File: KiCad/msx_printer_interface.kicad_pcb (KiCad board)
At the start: 2 copper layers, 65.7 x 54 mm, 12 parts, among them J1 MSX Cartridge Connector, J2 Conn_02x07_Top_Bottom, U1 ATF22V10C-15PU, U2 74HC273

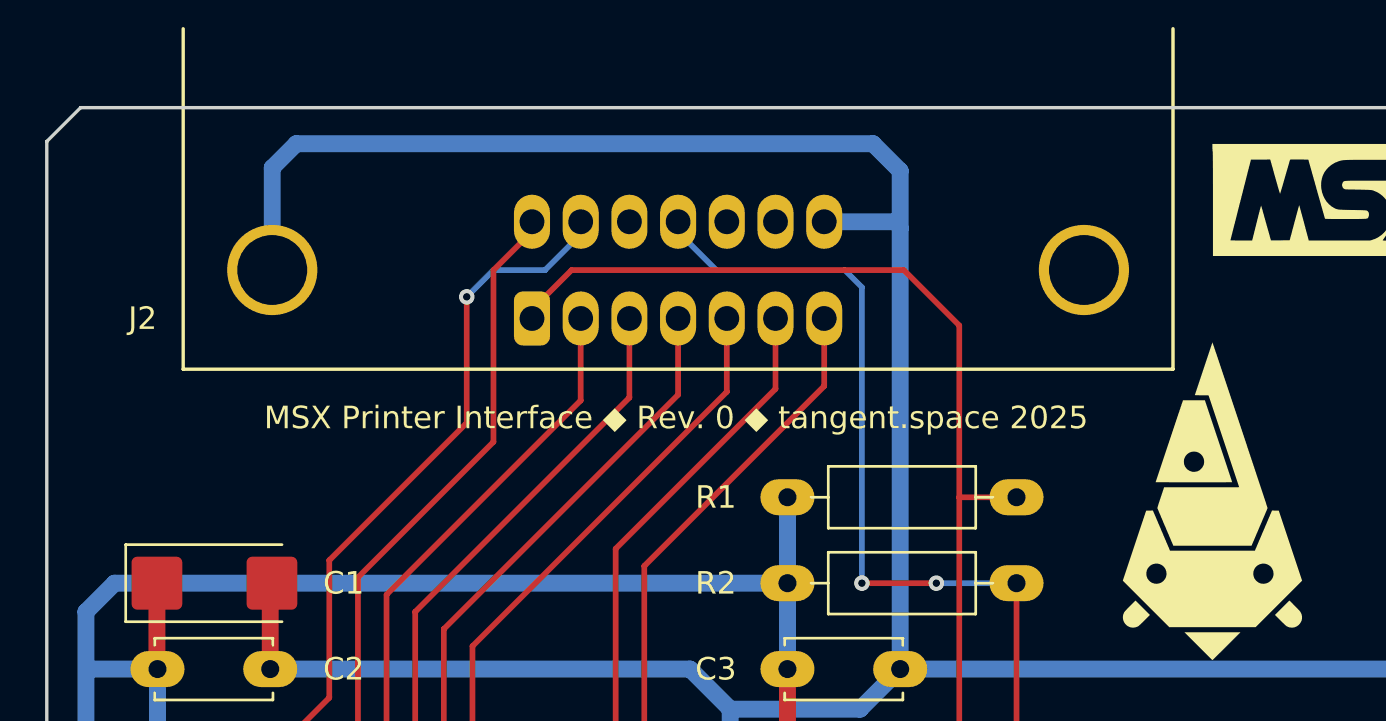
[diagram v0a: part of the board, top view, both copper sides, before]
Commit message: Adjust J2 ground
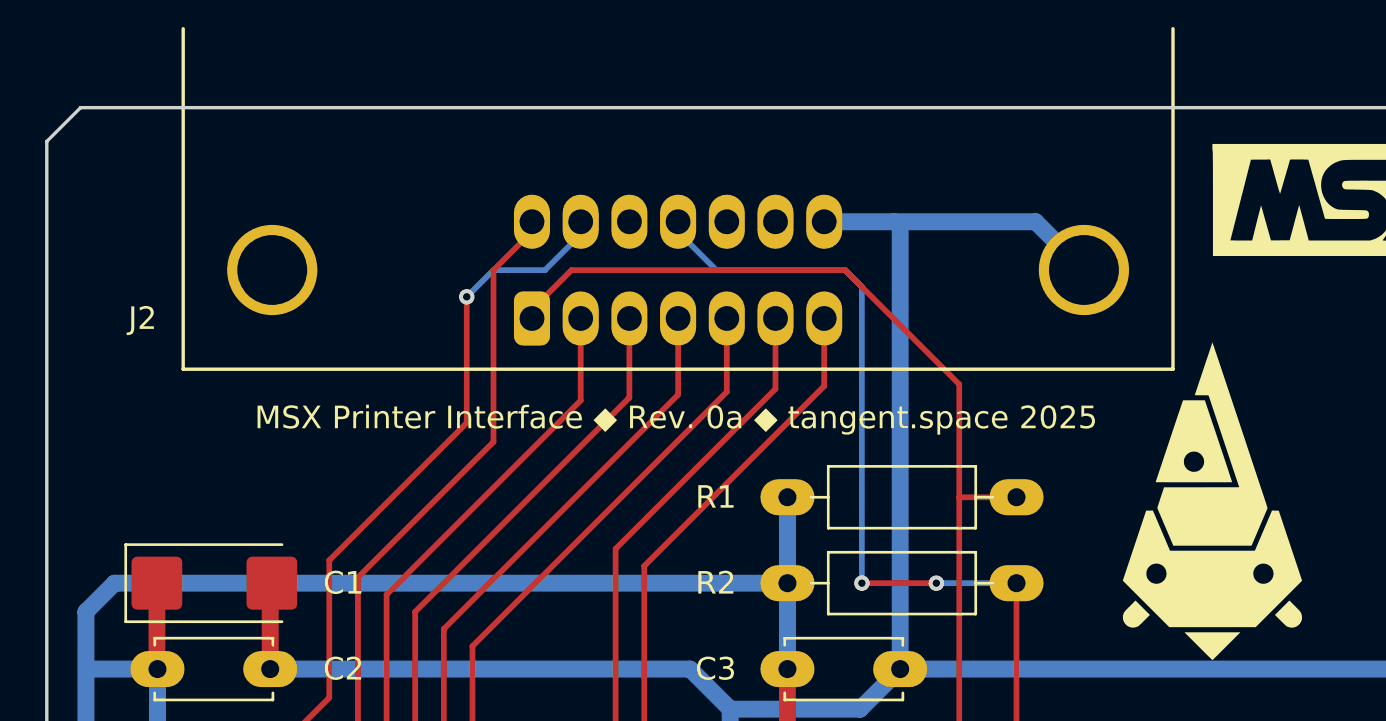
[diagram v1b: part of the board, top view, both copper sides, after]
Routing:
- net GND: track 180.1 -> 153.6 mm
- net #STROBE: track 42.3 -> 40.8 mm
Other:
- board text added: "MSX Printer Interface ◆ Rev. 0a ◆ tangent.space 2025"
- board text removed: "MSX Printer Interface ◆ Rev. 0 ◆ tangent.space 2025"
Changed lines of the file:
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@@
 			(layers "*.Cu" "*.Mask")
 			(remove_unused_layers no)
-			(net 2 "GND")
 		)
 		(pad "" thru_hole circle
@@
 			(layers "*.Cu" "*.Mask")
 			(remove_unused_layers no)
+			(net 2 "GND")
 		)
 		(pad "1" thru_hole roundrect
@@
 		(layer "Edge.Cuts")
 	)
-	(gr_text "MSX Printer Interface ◆ Rev. 0 ◆ tangent.space 2025"
+	(gr_text "MSX Printer Interface ◆ Rev. 0a ◆ tangent.space 2025"
 		(at 54.4125 17.255 0)
 		(layer "F.SilkS")
@@
 	)
 	(segment
-		(start 37.565 5.1)
-		(end 63.148 5.1)
-		(width 0.75)
-		(layer "B.Cu")
-		(net 2)
-	)
-	(segment
 		(start 37.795 44.875)
 		(end 39.03 43.64)
@@
 	)
 	(segment
-		(start 36.5 10.7)
-		(end 36.5 6.165)
+		(start 39.03 43.64)
+		(end 54.25 43.64)
 		(width 0.75)
 		(layer "B.Cu")
@@
 	)
 	(segment
-		(start 39.03 43.64)
-		(end 54.25 43.64)
+		(start 56.81 42.37)
+		(end 56.81 39.83)
 		(width 0.75)
 		(layer "B.Cu")
@@
 	)
 	(segment
-		(start 56.81 42.37)
-		(end 56.81 39.83)
+		(start 64.068 8.56)
+		(end 70.36 8.56)
 		(width 0.75)
 		(layer "B.Cu")
@@
 	)
 	(segment
+		(start 70.36 8.56)
+		(end 72.5 10.7)
+		(width 0.75)
+		(layer "B.Cu")
+		(net 2)
+	)
+	(segment
 		(start 62.572 30.178)
 		(end 64.35 28.4)
@@
 	)
 	(segment
-		(start 36.5 6.165)
-		(end 37.565 5.1)
-		(width 0.75)
-		(layer "B.Cu")
-		(net 2)
-	)
-	(segment
-		(start 63.148 5.1)
-		(end 64.35 6.302)
-		(width 0.75)
-		(layer "B.Cu")
-		(net 2)
-	)
-	(segment
 		(start 64.35 8.842)
 		(end 64.35 28.4)
@@
 	)
 	(segment
-		(start 64.35 6.302)
-		(end 64.35 8.842)
-		(width 0.75)
-		(layer "B.Cu")
-		(net 2)
-	)
-	(segment
 		(start 64.35 28.4)
 		(end 89.195 28.4)
@@
 	)
 	(segment
-		(start 61.89 10.705)
+		(start 61.905 10.705)
 		(end 56.195 10.705)
 		(width 0.254)
@@
 	)
 	(segment
-		(start 62.652 11.467)
-		(end 61.89 10.705)
+		(start 62.652 11.452)
+		(end 61.905 10.705)
 		(width 0.254)
 		(layer "B.Cu")
@@
 	)
 	(segment
-		(start 62.652 24.59)
-		(end 62.652 11.467)
+		(start 69.51 24.59)
+		(end 65.954 24.59)
 		(width 0.254)
 		(layer "B.Cu")
@@
 	)
 	(segment
-		(start 69.51 24.59)
-		(end 65.954 24.59)
+		(start 62.652 24.59)
+		(end 62.652 11.452)
 		(width 0.254)
 		(layer "B.Cu")
@@
 	)
 	(segment
-		(start 64.515 10.705)
-		(end 66.97 13.16)
+		(start 61.905 10.705)
+		(end 66.97 15.77)
 		(width 0.254)
 		(layer "F.Cu")
@@
 	(segment
 		(start 49.775 10.705)
-		(end 64.515 10.705)
+		(end 61.905 10.705)
 		(width 0.254)
 		(layer "F.Cu")
@@
 	)
 	(segment
-		(start 69.51 20.78)
+		(start 66.97 15.77)
 		(end 66.97 20.78)
 		(width 0.254)
@@
 	)
 	(segment
-		(start 48.02 12.46)
-		(end 49.775 10.705)
+		(start 69.51 20.78)
+		(end 66.97 20.78)
 		(width 0.254)
 		(layer "F.Cu")
@@
 	)
 	(segment
-		(start 66.97 20.78)
-		(end 66.97 13.16)
+		(start 48.02 12.46)
+		(end 49.775 10.705)
 		(width 0.254)
 		(layer "F.Cu")

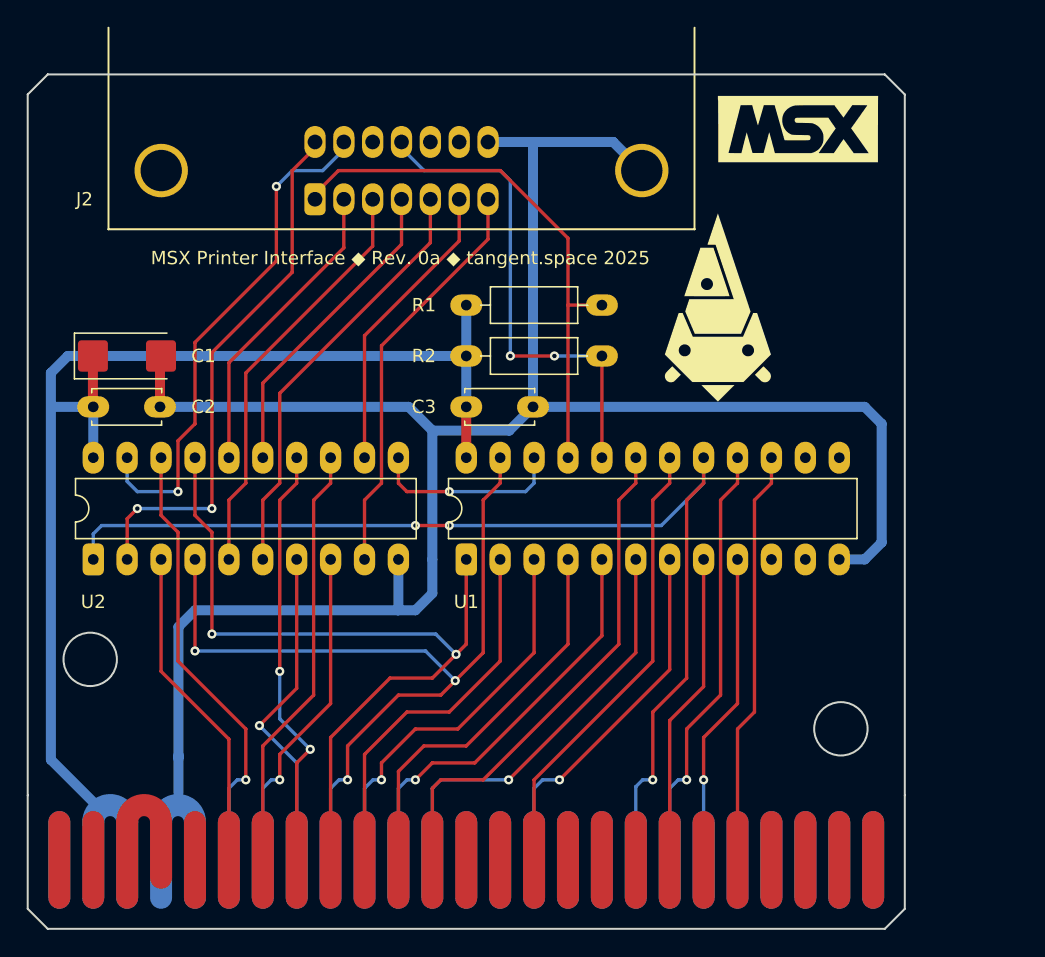
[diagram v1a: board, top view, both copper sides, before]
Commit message: Routing changes
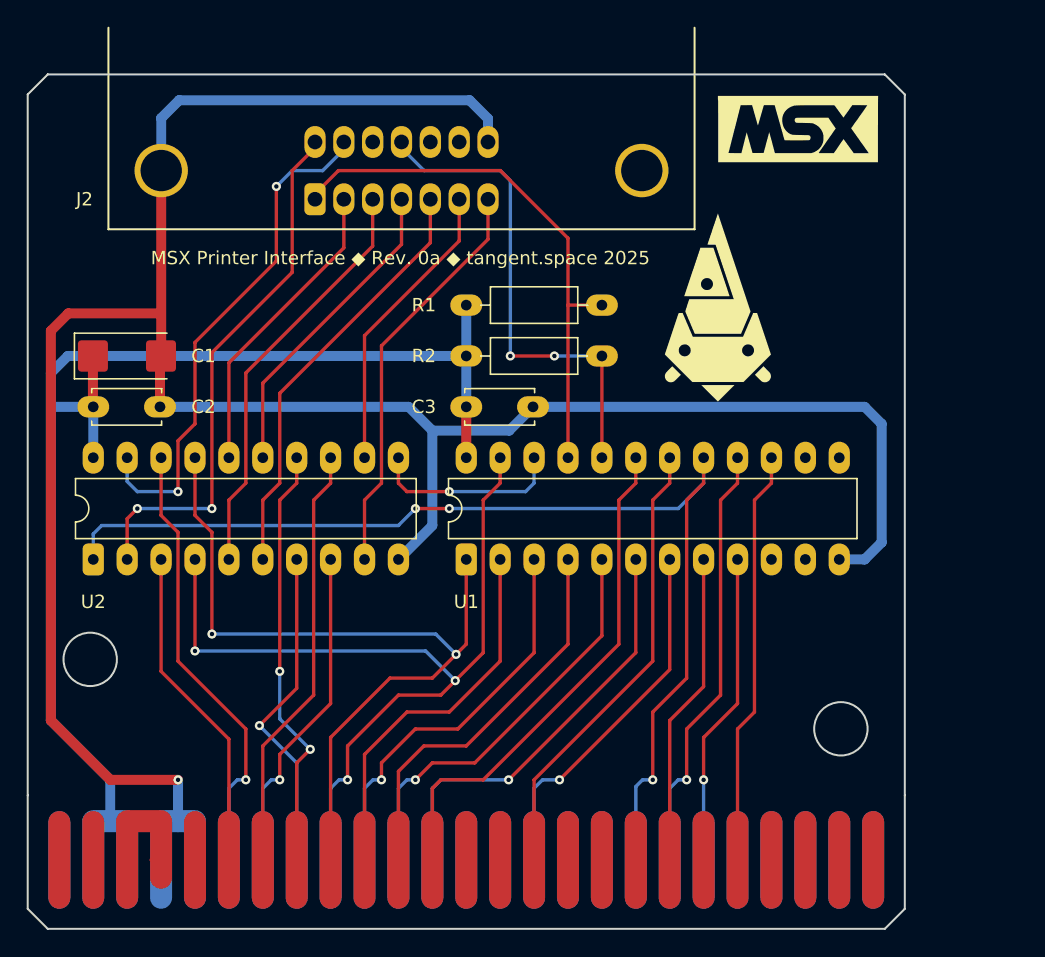
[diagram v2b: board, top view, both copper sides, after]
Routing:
- net GND: track 153.6 -> 183.1 mm, vias 0 -> 1
- net Net-(J1-Pin_44): track 0.00 -> 3.60 mm
- net VCC: track 88.4 -> 91.5 mm
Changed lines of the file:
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@@
 		(allow_soldermask_bridges_in_footprints no)
 		(tenting front back)
+		(grid_origin 89.83 0)
 		(pcbplotparams
 			(layerselection 0x00000000_00000000_00000000_0200a0a5)
@@
 			(layers "*.Cu" "*.Mask")
 			(remove_unused_layers no)
+			(net 2 "GND")
 		)
 		(pad "" thru_hole circle
@@
 			(layers "*.Cu" "*.Mask")
 			(remove_unused_layers no)
-			(net 2 "GND")
 		)
 		(pad "1" thru_hole roundrect
@@
 		(embedded_fonts no)
 	)
-	(gr_arc
-		(start 33.95 59.5)
-		(mid 35.22 58.23)
-		(end 36.49 59.5)
-		(stroke
-			(width 1.65)
-			(type solid)
-		)
-		(layer "F.Cu")
-		(net 26)
-	)
-	(gr_arc
-		(start 31.41 59.5)
-		(mid 32.68 58.23)
-		(end 33.95 59.5)
-		(stroke
-			(width 1.65)
-			(type solid)
-		)
-		(layer "B.Cu")
-		(net 1)
-	)
-	(gr_arc
-		(start 36.49 59.5)
-		(mid 37.76 58.23)
-		(end 39.03 59.5)
-		(stroke
-			(width 1.65)
-			(type solid)
-		)
-		(layer "B.Cu")
-		(net 2)
-	)
 	(gr_line
 		(start 28 3.5)
@@
 	)
 	(segment
-		(start 29.505 24.59)
-		(end 28.235 25.86)
+		(start 31.41 28.4)
+		(end 28.485 28.4)
 		(width 0.75)
 		(layer "B.Cu")
@@
 	)
 	(segment
-		(start 28.235 54.835)
-		(end 31.63 58.23)
+		(start 28.235 25.86)
+		(end 28.235 51.8922)
 		(width 0.75)
 		(layer "B.Cu")
@@
 	)
 	(segment
-		(start 31.41 28.4)
-		(end 28.485 28.4)
+		(start 32.68 56.3372)
+		(end 32.68 59.436)
 		(width 0.75)
 		(layer "B.Cu")
@@
 	)
 	(segment
-		(start 28.235 25.86)
-		(end 28.235 54.835)
+		(start 59.35 24.59)
+		(end 29.505 24.59)
 		(width 0.75)
 		(layer "B.Cu")
@@
 	)
 	(segment
-		(start 31.63 58.23)
-		(end 32.68 58.23)
+		(start 28.235 51.8922)
+		(end 32.68 56.3372)
 		(width 0.75)
 		(layer "B.Cu")
@@
 	)
 	(segment
-		(start 59.35 24.59)
-		(end 29.505 24.59)
+		(start 33.95 59.436)
+		(end 31.41 59.436)
+		(width 1.65)
+		(layer "B.Cu")
+		(net 1)
+	)
+	(segment
+		(start 29.505 24.59)
+		(end 28.235 25.86)
 		(width 0.75)
 		(layer "B.Cu")
@@
 	)
 	(segment
-		(start 36.41 24.665)
-		(end 36.41 28.4)
+		(start 28.235 22.7076)
+		(end 29.5431 21.3995)
 		(width 0.75)
 		(layer "F.Cu")
@@
 	)
 	(segment
-		(start 54.25 43.64)
-		(end 55.54 43.64)
+		(start 36.5 10.7)
+		(end 36.5 24.575)
 		(width 0.75)
-		(layer "B.Cu")
+		(layer "F.Cu")
 		(net 2)
 	)
 	(segment
-		(start 37.795 44.875)
-		(end 39.03 43.64)
+		(start 37.76 56.34)
+		(end 32.6828 56.34)
 		(width 0.75)
-		(layer "B.Cu")
+		(layer "F.Cu")
 		(net 2)
 	)
 	(segment
-		(start 90.465 38.56)
-		(end 89.195 39.83)
+		(start 36.485 10.715)
+		(end 36.5 10.7)
 		(width 0.75)
-		(layer "B.Cu")
+		(layer "F.Cu")
 		(net 2)
 	)
 	(segment
-		(start 37.76 57.365)
-		(end 37.795 57.33)
-		(width 0.254)
-		(layer "B.Cu")
+		(start 32.6828 56.34)
+		(end 28.235 51.8922)
+		(width 0.75)
+		(layer "F.Cu")
 		(net 2)
 	)
 	(segment
-		(start 55.54 43.64)
-		(end 56.81 42.37)
+		(start 36.5 24.575)
+		(end 36.485 24.59)
 		(width 0.75)
-		(layer "B.Cu")
+		(layer "F.Cu")
 		(net 2)
 	)
 	(segment
-		(start 64.068 8.56)
-		(end 64.35 8.842)
-		(width 0.254)
-		(layer "B.Cu")
+		(start 36.41 24.665)
+		(end 36.41 28.4)
+		(width 0.75)
+		(layer "F.Cu")
 		(net 2)
 	)
 	(segment
-		(start 56.81 39.83)
-		(end 56.81 30.178)
+		(start 28.235 51.8922)
+		(end 28.235 22.7076)
 		(width 0.75)
-		(layer "B.Cu")
+		(layer "F.Cu")
 		(net 2)
 	)
 	(segment
-		(start 55.032 28.4)
-		(end 56.81 30.178)
+		(start 29.5431 21.3995)
+		(end 36.3707 21.3995)
 		(width 0.75)
+		(layer "F.Cu")
+		(net 2)
+	)
+	(via
+		(at 37.76 56.34)
+		(size 0.6858)
+		(drill 0.3302)
+		(layers "F.Cu" "B.Cu")
+		(net 2)
+	)
+	(segment
+		(start 39.03 59.436)
+		(end 37.76 59.436)
+		(width 1.65)
 		(layer "B.Cu")
 		(net 2)
 	)
 	(segment
-		(start 54.27 39.83)
-		(end 54.27 43.62)
+		(start 37.76 56.34)
+		(end 37.76 59.436)
 		(width 0.75)
 		(layer "B.Cu")
@@
 	)
 	(segment
-		(start 90.465 29.67)
-		(end 90.465 38.56)
+		(start 37.8362 5.4356)
+		(end 59.604 5.4356)
 		(width 0.75)
 		(layer "B.Cu")
@@
 	)
 	(segment
-		(start 39.03 43.64)
-		(end 54.25 43.64)
+		(start 54.27 39.83)
+		(end 56.81 37.29)
 		(width 0.75)
 		(layer "B.Cu")
@@
 	)
 	(segment
-		(start 56.81 42.37)
-		(end 56.81 39.83)
-		(width 0.75)
+		(start 37.76 59.436)
+		(end 36.49 59.436)
+		(width 1.65)
 		(layer "B.Cu")
 		(net 2)
 	)
 	(segment
-		(start 64.068 8.56)
-		(end 70.36 8.56)
+		(start 90.465 38.56)
+		(end 89.195 39.83)
 		(width 0.75)
 		(layer "B.Cu")
@@
 	)
 	(segment
-		(start 60.98 8.56)
-		(end 64.068 8.56)
+		(start 55.032 28.4)
+		(end 56.81 30.178)
 		(width 0.75)
 		(layer "B.Cu")
@@
 	)
 	(segment
-		(start 54.27 43.62)
-		(end 54.25 43.64)
+		(start 90.465 29.67)
+		(end 90.465 38.56)
 		(width 0.75)
 		(layer "B.Cu")
@@
 	)
 	(segment
-		(start 70.36 8.56)
-		(end 72.5 10.7)
+		(start 36.5 6.7718)
+		(end 37.8362 5.4356)
 		(width 0.75)
 		(layer "B.Cu")
@@
 	)
 	(segment
-		(start 37.795 54.75)
-		(end 37.795 44.875)
+		(start 59.604 5.4356)
+		(end 60.98 6.8116)
 		(width 0.75)
 		(layer "B.Cu")
@@
 	)
 	(segment
-		(start 37.795 54.5)
-		(end 37.795 57.33)
+		(start 56.81 37.29)
+		(end 56.81 30.178)
 		(width 0.75)
 		(layer "B.Cu")
@@
 	)
 	(segment
-		(start 64.35 8.842)
-		(end 64.35 28.4)
+		(start 36.41 28.4)
+		(end 55.032 28.4)
 		(width 0.75)
 		(layer "B.Cu")
@@
 	)
 	(segment
-		(start 36.41 28.4)
-		(end 55.032 28.4)
+		(start 64.35 28.4)
+		(end 89.195 28.4)
 		(width 0.75)
 		(layer "B.Cu")
@@
 	)
 	(segment
-		(start 64.35 28.4)
-		(end 89.195 28.4)
+		(start 60.98 6.8116)
+		(end 60.98 8.56)
+		(width 0.75)
+		(layer "B.Cu")
+		(net 2)
+	)
+	(segment
+		(start 36.5 10.7)
+		(end 36.5 6.7718)
 		(width 0.75)
 		(layer "B.Cu")
@@
 	)
 	(segment
+		(start 33.95 59.436)
+		(end 36.49 59.436)
+		(width 1.65)
+		(layer "F.Cu")
+		(net 26)
+	)
+	(segment
+		(start 35.74 62.3375)
+		(end 36.49 61.5875)
+		(width 0.254)
+		(layer "F.Cu")
+		(net 26)
+	)
+	(segment
 		(start 73.32 51.26)
 		(end 75.86 48.72)
@@
 	)
 	(segment
-		(start 77.13 34.115)
-		(end 77.13 32.21)
+		(start 55.54 36.02)
+		(end 58.08 36.02)
 		(width 0.254)
 		(layer "F.Cu")
@@
 	)
 	(segment
-		(start 75.86 48.72)
-		(end 75.86 35.385)
+		(start 77.13 34.115)
+		(end 77.13 32.21)
 		(width 0.254)
 		(layer "F.Cu")
@@
 	)
 	(segment
-		(start 58.08 37.29)
-		(end 55.54 37.29)
+		(start 75.86 48.72)
+		(end 75.86 35.385)
 		(width 0.254)
 		(layer "F.Cu")
@@
 	)
 	(via
-		(at 58.08 37.29)
+		(at 58.08 36.02)
 		(size 0.6858)
 		(drill 0.3302)
@@
 	)
 	(via
-		(at 55.54 37.29)
+		(at 55.54 36.02)
 		(size 0.6858)
 		(drill 0.3302)
@@
 	)
 	(segment
-		(start 58.08 37.29)
-		(end 73.955 37.29)
+		(start 54.27 37.29)
+		(end 32.045 37.29)
 		(width 0.254)
 		(layer "B.Cu")
@@
 	)
 	(segment
-		(start 55.54 37.29)
-		(end 32.045 37.29)
+		(start 58.08 36.02)
+		(end 75.225 36.02)
 		(width 0.254)
 		(layer "B.Cu")
@@
 	)
 	(segment
-		(start 77.13 34.115)
-		(end 77.13 32.21)
+		(start 75.225 36.02)
+		(end 77.13 34.115)
 		(width 0.254)
 		(layer "B.Cu")
@@
 	)
 	(segment
-		(start 72.05 56.848)
-		(end 72.05 63)
+		(start 55.54 36.02)
+		(end 54.27 37.29)
 		(width 0.254)
 		(layer "B.Cu")
@@
 	)
 	(segment
-		(start 73.955 37.29)
-		(end 77.13 34.115)
+		(start 72.05 56.848)
+		(end 72.05 63)
 		(width 0.254)
 		(layer "B.Cu")
@@
 	)
 	(segment
-		(start 31.41 37.925)
-		(end 31.41 39.83)
+		(start 77.13 34.115)
+		(end 77.13 32.21)
 		(width 0.254)
 		(layer "B.Cu")
@@
 		(width 0.254)
 		(layer "B.Cu")
+		(net 43)
+	)
+	(segment
+		(start 31.41 37.925)
+		(end 31.41 39.83)
+		(width 0.254)
+		(layer "B.Cu")

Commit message: Silkscreen
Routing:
- net GND: track 183.1 -> 174.7 mm
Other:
- board text added: "◆ WARNING: Do not use in machines with existing printer interface! ◆"
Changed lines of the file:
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@@
+		)
+	)
+	(gr_text "◆ WARNING: Do not use in machines with existing printer interface! ◆"
+		(at 32.201189 58.293 0)
+		(layer "F.SilkS")
+		(effects
+			(font
+				(size 1 1)
+				(thickness 0.15)
+			)
+			(justify left bottom)
 		)
 	)
@@
 	)
 	(segment
-		(start 28.235 22.7076)
-		(end 29.5431 21.3995)
-		(width 0.75)
-		(layer "F.Cu")
-		(net 2)
-	)
-	(segment
 		(start 36.5 10.7)
-		(end 36.5 24.575)
+		(end 36.5 19.939)
+		(width 0.75)
+		(layer "F.Cu")
+		(net 2)
+	)
+	(segment
+		(start 29.5304 20.9042)
+		(end 36.4746 20.9042)
 		(width 0.75)
 		(layer "F.Cu")
@@
 	)
 	(segment
+		(start 36.5 19.939)
+		(end 36.5 24.575)
+		(width 0.75)
+		(layer "F.Cu")
+		(net 2)
+	)
+	(segment
 		(start 32.6828 56.34)
 		(end 28.235 51.8922)
@@
 	)
 	(segment
+		(start 28.235 22.1996)
+		(end 29.5304 20.9042)
+		(width 0.75)
+		(layer "F.Cu")
+		(net 2)
+	)
+	(segment
 		(start 28.235 51.8922)
-		(end 28.235 22.7076)
-		(width 0.75)
-		(layer "F.Cu")
-		(net 2)
-	)
-	(segment
-		(start 29.5431 21.3995)
-		(end 36.3707 21.3995)
+		(end 28.235 22.1996)
 		(width 0.75)
 		(layer "F.Cu")
@@
 	)
 	(segment
-		(start 37.8362 5.4356)
-		(end 59.604 5.4356)
-		(width 0.75)
-		(layer "B.Cu")
-		(net 2)
-	)
-	(segment
 		(start 54.27 39.83)
 		(end 56.81 37.29)
@@
 	)
 	(segment
-		(start 36.5 6.7718)
-		(end 37.8362 5.4356)
+		(start 62.703 8.56)
+		(end 60.98 8.56)
 		(width 0.75)
 		(layer "B.Cu")
@@
 	)
 	(segment
-		(start 59.604 5.4356)
-		(end 60.98 6.8116)
+		(start 64.35 28.4)
+		(end 64.35 10.207)
+		(width 0.75)
+		(layer "B.Cu")
+		(net 2)
+	)
+	(segment
+		(start 64.35 10.207)
+		(end 62.703 8.56)
 		(width 0.75)
 		(layer "B.Cu")
@@
 		(width 0.75)
 		(layer "B.Cu")
-		(net 2)
-	)
-	(segment
-		(start 60.98 6.8116)
-		(end 60.98 8.56)
-		(width 0.75)
-		(layer "B.Cu")
-		(net 2)
-	)
-	(segment
-		(start 36.5 10.7)
-		(end 36.5 6.7718)
-		(width 0.75)
-		(layer "B.Cu")

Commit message: Update msx_printer_interface.kicad_pcb
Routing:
- net GND: track 174.7 -> 189.7 mm, vias 1 -> 2
- net BUSY: track 36.8 -> 34.2 mm, vias 2 -> 0
- net CLK_DATA: vias 1 -> 0
- net #RESET: vias 3 -> 1
